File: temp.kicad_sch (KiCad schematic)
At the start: 1 part, among them U2 MCP9808-E/MS

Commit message: first
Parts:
- added C1: 1uF, symbol Device:C_Small_US
- added J1: Conn_01x02_Pin, Package_SO:SOIC-16_3.9x9.9mm_P1.27mm, symbol Connector:Conn_01x02_Pin
- added R1: 0805W8F4702T5E, EasyEDA:R0805, symbol EasyEDA:0805W8F4702T5E
- added U3: LMT84LPM, EasyEDA:TO-92-3_L4.9-W3.7-P2.54-L, symbol EasyEDA:LMT84LPM
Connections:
- net LMT84_OUT: now also U3.2 (OUT)
- net NTC_MID: now also J1.1 (Pin_1), R1.2
- net GND: now reaches U2.4 (GND)
- net GND: now also U2.5 (A2), U2.6 (A1), U2.7 (A0), C1.1, J1.2 (Pin_2), U3.3 (GND)
- net +3V3: now reaches U2.8 (VDD)
- net +3V3: now also C1.2, R1.1, U3.1 (VDD)

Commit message: small modifications
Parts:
- removed C1: 1uF, symbol Device:C_Small_US
- added C501, C502: 0.1uF, EasyEDA:C0603, symbol HAB5OBC:CC0603KRX7R9BB104
- J501: renamed from J1; value Conn_01x02_Pin -> NTC
- R501: renamed from R1; value 0805W8F4702T5E -> 47k
- renumbered U3 to U501, U2 to U502
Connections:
- net +3V3: now also C502.1
- net GND: now also C501.1, C502.2
- net NTC_MID: now also C501.2
- no-connect marks 0 -> 1
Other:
- moved on the sheet: J501, R501, U502

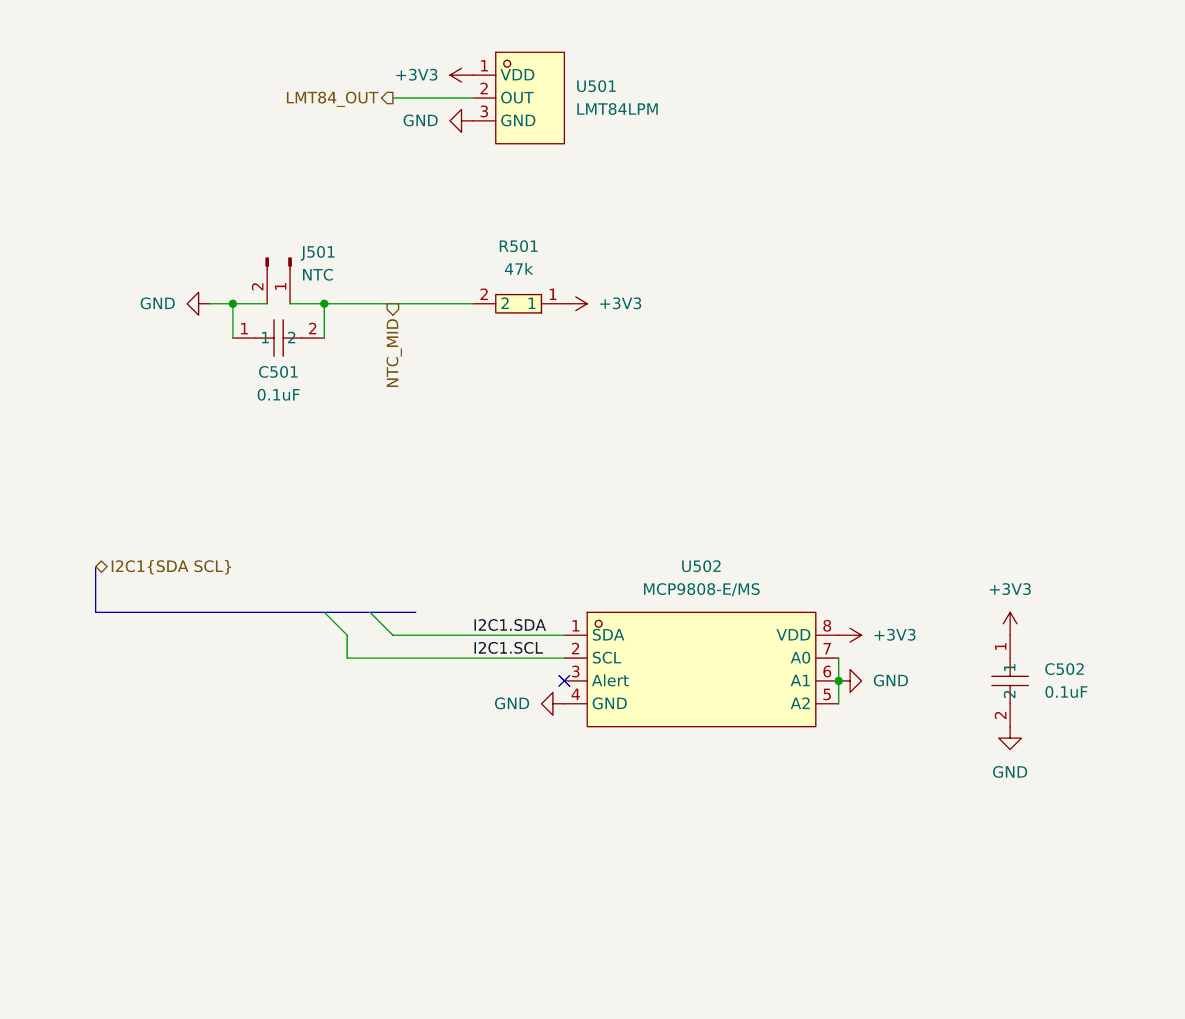
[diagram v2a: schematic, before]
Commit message: change power references and cap placement
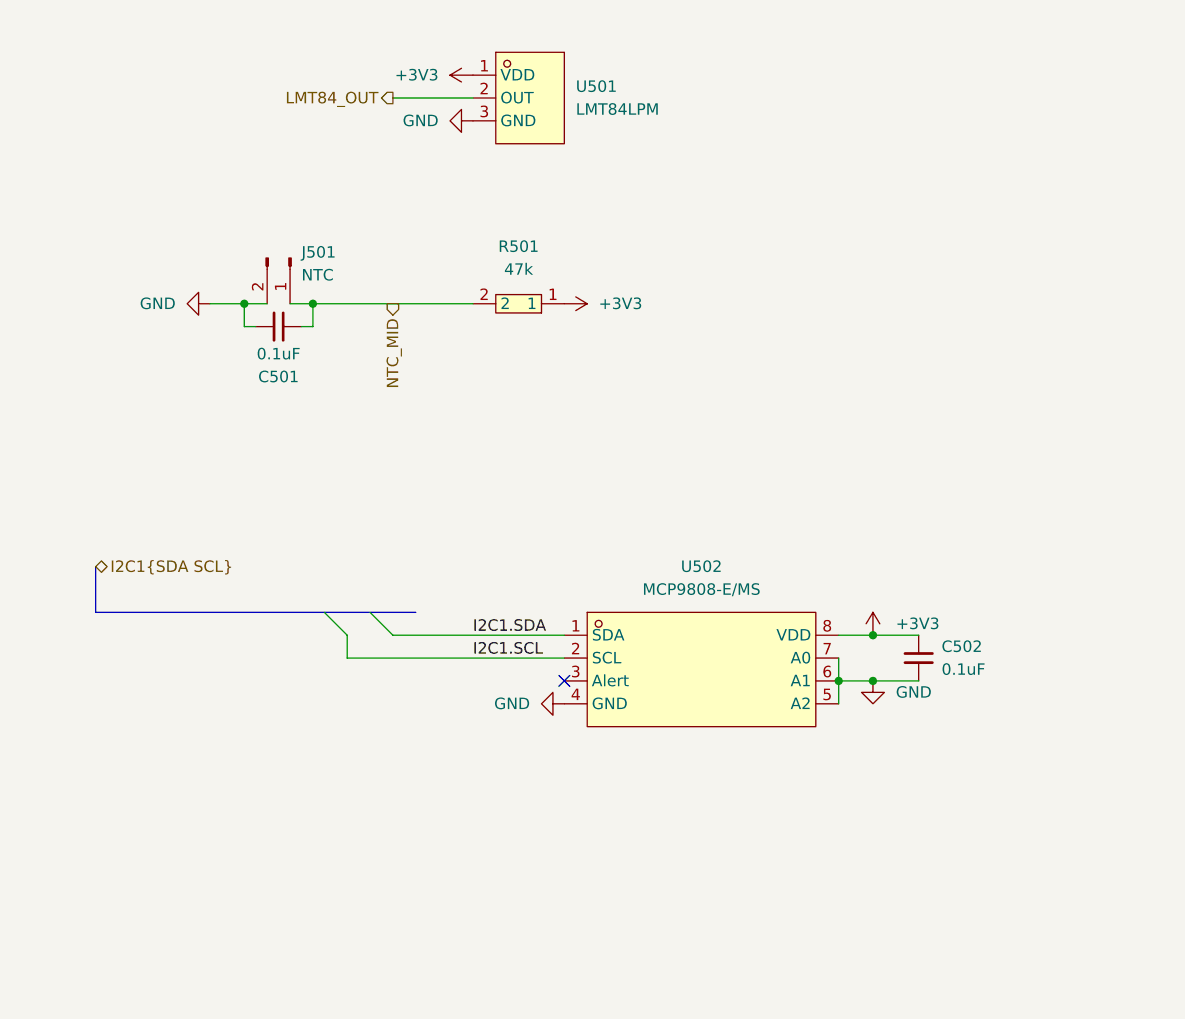
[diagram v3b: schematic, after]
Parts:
- C501, C502: symbol HAB5OBC:CC0603KRX7R9BB104 -> Device:C_Small
